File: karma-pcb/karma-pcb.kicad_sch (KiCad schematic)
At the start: 78 parts, among them J3 BAT, U1 xiao-ble, U2 xiao-ble

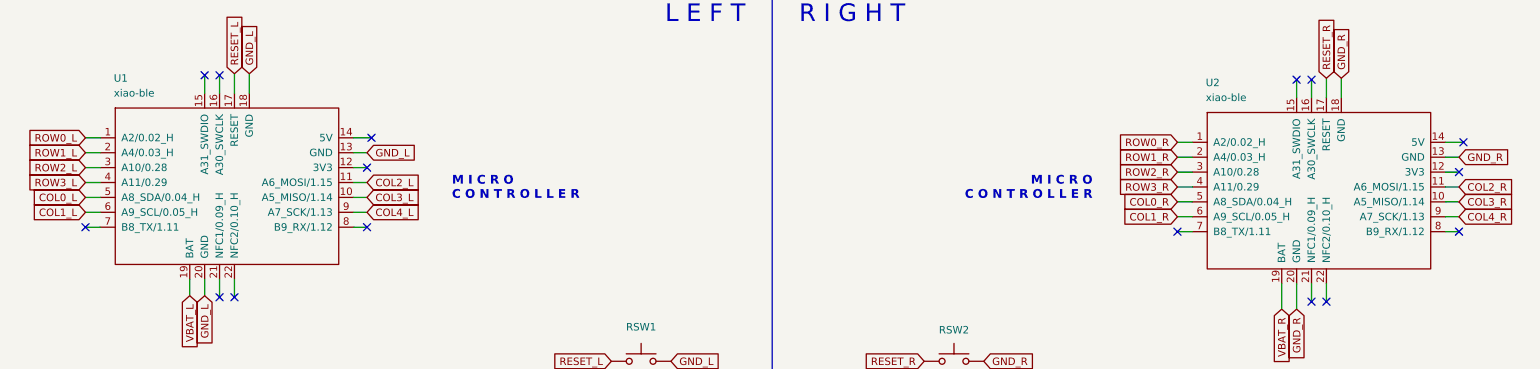
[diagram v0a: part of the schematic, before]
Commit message: Update schema to rev 0.2
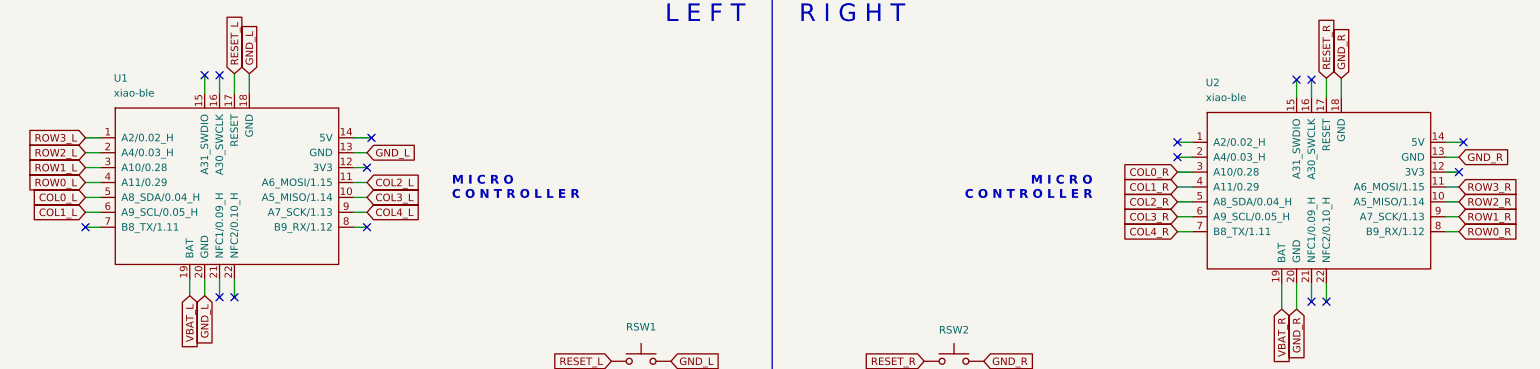
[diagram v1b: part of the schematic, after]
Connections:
- net COL0_R: now also U2.3 (A10/0.28); no longer U2.5 (A8_SDA/0.04_H)
- net COL1_R: now also U2.4 (A11/0.29); no longer U2.6 (A9_SCL/0.05_H)
- net COL2_R: now also U2.5 (A8_SDA/0.04_H); no longer U2.11 (A6_MOSI/1.15)
- net COL3_R: now also U2.6 (A9_SCL/0.05_H); no longer U2.10 (A5_MISO/1.14)
- net COL4_R: now also U2.7 (B8_TX/1.11); no longer U2.9 (A7_SCK/1.13)
- net ROW0_L: now also U1.4 (A11/0.29); no longer U1.1 (A2/0.02_H)
- net ROW0_R: now also U2.8 (B9_RX/1.12); no longer U2.1 (A2/0.02_H)
- net ROW1_L: now also U1.3 (A10/0.28); no longer U1.2 (A4/0.03_H)
- net ROW1_R: now also U2.9 (A7_SCK/1.13); no longer U2.2 (A4/0.03_H)
- net ROW2_L: now also U1.2 (A4/0.03_H); no longer U1.3 (A10/0.28)
- net ROW2_R: now also U2.10 (A5_MISO/1.14); no longer U2.3 (A10/0.28)
- net ROW3_L: now also U1.1 (A2/0.02_H); no longer U1.4 (A11/0.29)
- net ROW3_R: now also U2.11 (A6_MOSI/1.15); no longer U2.4 (A11/0.29)
